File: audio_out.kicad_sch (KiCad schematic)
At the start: 34 parts, among them SW2 Gain0, SW3 Gain1, U3 PAM8908JER, U4 PCM5102A, U8 AP7333-33SRG-7

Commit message: Reviewing every item in the BOM against LCSC database. Found several errors already. Part way done.
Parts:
- C21, C22, C25, C27, C30, C31, C36, C37, C38, C39, C41, C42, C43: DPFNOTES (none) -> 25V 1uF X5R ±10% 0402 Multilayer Ceramic Capacitors MLCC - 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; JLC Basic Part (none) -> Basic
- C23, C24, C40: DPFNOTES (none) -> 50V 2.2uF X5R ±10% 0805 Multilayer Ceramic Capacitors MLCC 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; JLC Basic Part (none) -> Basic; Manu Part (none) -> CL21A225KBQNNNE
- C26, C28, C32, C33: DPFNOTES (none) -> 50V 100nF X7R ±10% 0402 Multilayer Ceramic Capacitors MLCC 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; JLC Basic Part (none) -> Basic
- C29, C34, C35: JLC Basic Part (none) -> Basic
- R21: JLC Basic Part (none) -> Basic; Manu Part (none) -> 0402WGF1002TCE; Manufacturer (none) -> UNI-ROYAL(Uniroyal Elec)

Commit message: Finished checking all parts against LCSC IDs. Found remaining errors. Added manufacturer part numbers to all parts.
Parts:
- C21, C22, C25, C27, C30, C31, C36, C37, C38, C39, C41, C42, C43: Manu Part (none) -> CL05A105KA5NQNC; Manufacturer (none) -> Samsung Electro-Mechanics
- C23, C24, C40: Manufacturer (none) -> Samsung Electro-Mechanics
- C26, C28, C32, C33: Manu Part (none) -> CL05B104KB54PNC; Manufacturer (none) -> Samsung Electro-Mechanics
- C29: Manu Part (none) -> CL10A106MA8NRNC; Manufacturer (none) -> Samsung Electro-Mechanics
- C34, C35: Manu Part (none) -> CL05B103KB5NNNC; Manufacturer (none) -> Samsung Electro-Mechanics
- R22, R23: JLC Basic Part (none) -> Basic; Manu Part (none) -> 0402WGF2200TCE; Manufacturer (none) -> UNI-ROYAL(Uniroyal Elec)
- R24, R25: JLC Basic Part (none) -> Extended; Manu Part (none) -> 0402WGF3901TCE; Manufacturer (none) -> UNI-ROYAL(Uniroyal Elec)
- RN1: JLC Basic Part (none) -> Extended; Manu Part (none) -> 4D03WGJ0560T5E; Manufacturer (none) -> UNI-ROYAL(Uniroyal Elec)
- SW2, SW3: DPFNOTES ALPSALPINE SSSS811101, Like C&K PCM-12-SMT PCM12SMTR -> ALPSALPINE SSSS811101, Like C&K PCM-12-SMT PCM12SMTR --- 30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; JLC Basic Part (none) -> Extended; Manu Part (none) -> SSSS811101; Manufacturer (none) -> ALPSALPINE
- U3: JLC Basic Part (none) -> Extended; Manu Part (none) -> PAM8908JER; Manufacturer (none) -> Diodes Incorporated
- U4: JLC Basic Part (none) -> Extended; Manu Part (none) -> PCM5102APWR; Manufacturer (none) -> Texas Instruments
- U8: DPFNOTES (none) -> 300mA 65dB@(100Hz) Fixed 3.3V Positive electrode 6V SOT-23 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; JLC Basic Part (none) -> Extended; Manu Part (none) -> AP7333-33SRG-7; Manufacturer (none) -> Diodes Incorporated

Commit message: Update schematic with notes on the headphone amplifier and I2S MCK
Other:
- note added: "Datasheet"
- note added: "Pimoroni"
- note added: "Pimoroni used a different INx- configuration; this is from the datasheet."
- note added: "Pullup to unmute audio when AUDIO_MUTE not driven"
- note added: "This chip does not need MCK. Leave it disconnected for simplicity."
- note added: "Why does Pimoroni use R1-4 on line inputs from PCM5102A DAC?"
- moved on the sheet: R21

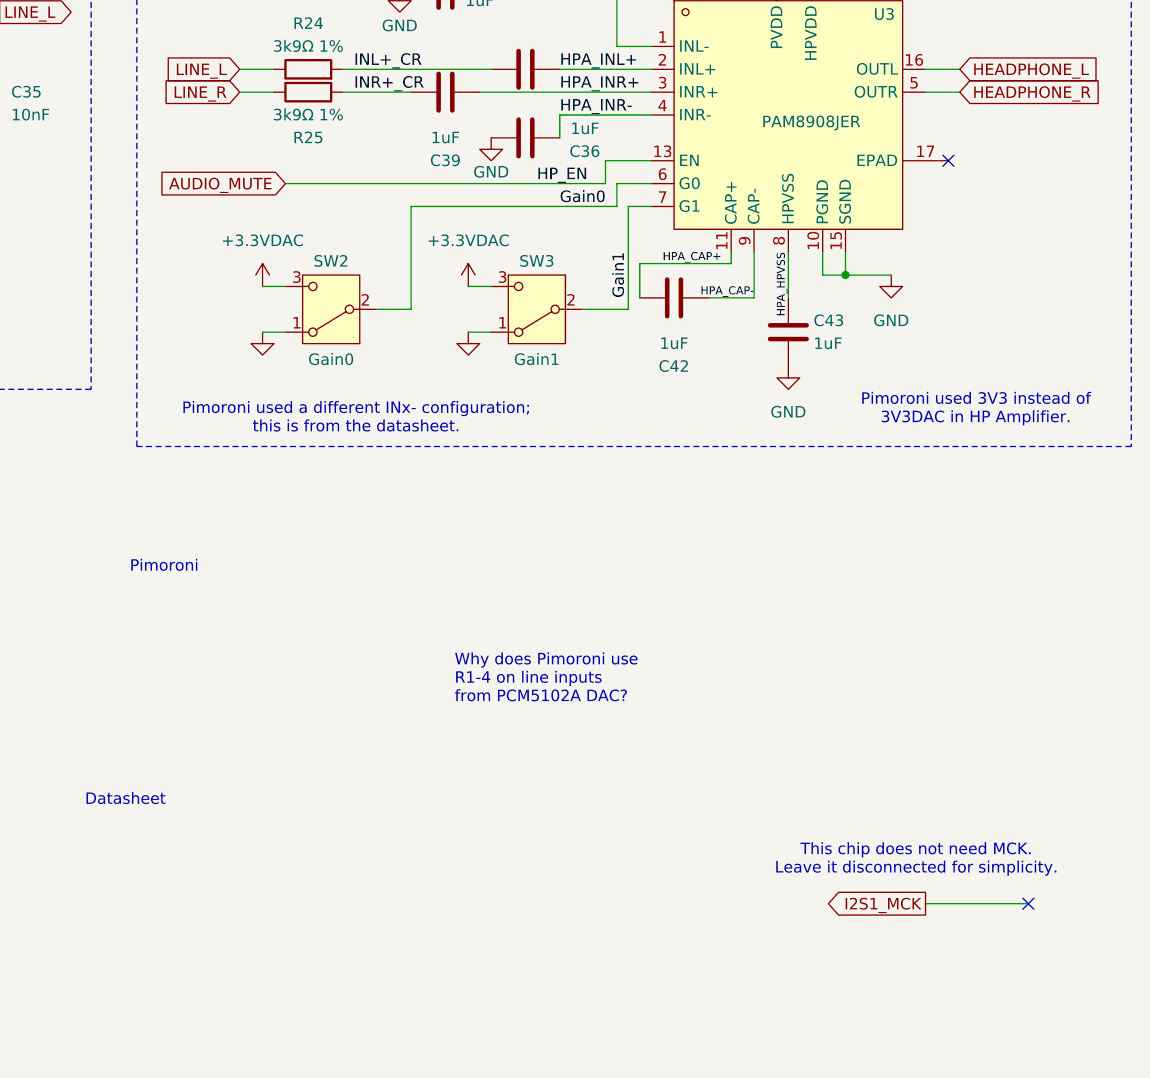
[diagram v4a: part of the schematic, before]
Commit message: More revisions for EVT2: 1. Move GAIN0/1 to MCU pins. 2. Revise SPI header with additional screen GPIO. 3. Revise GPIO header due to 1 and 2.
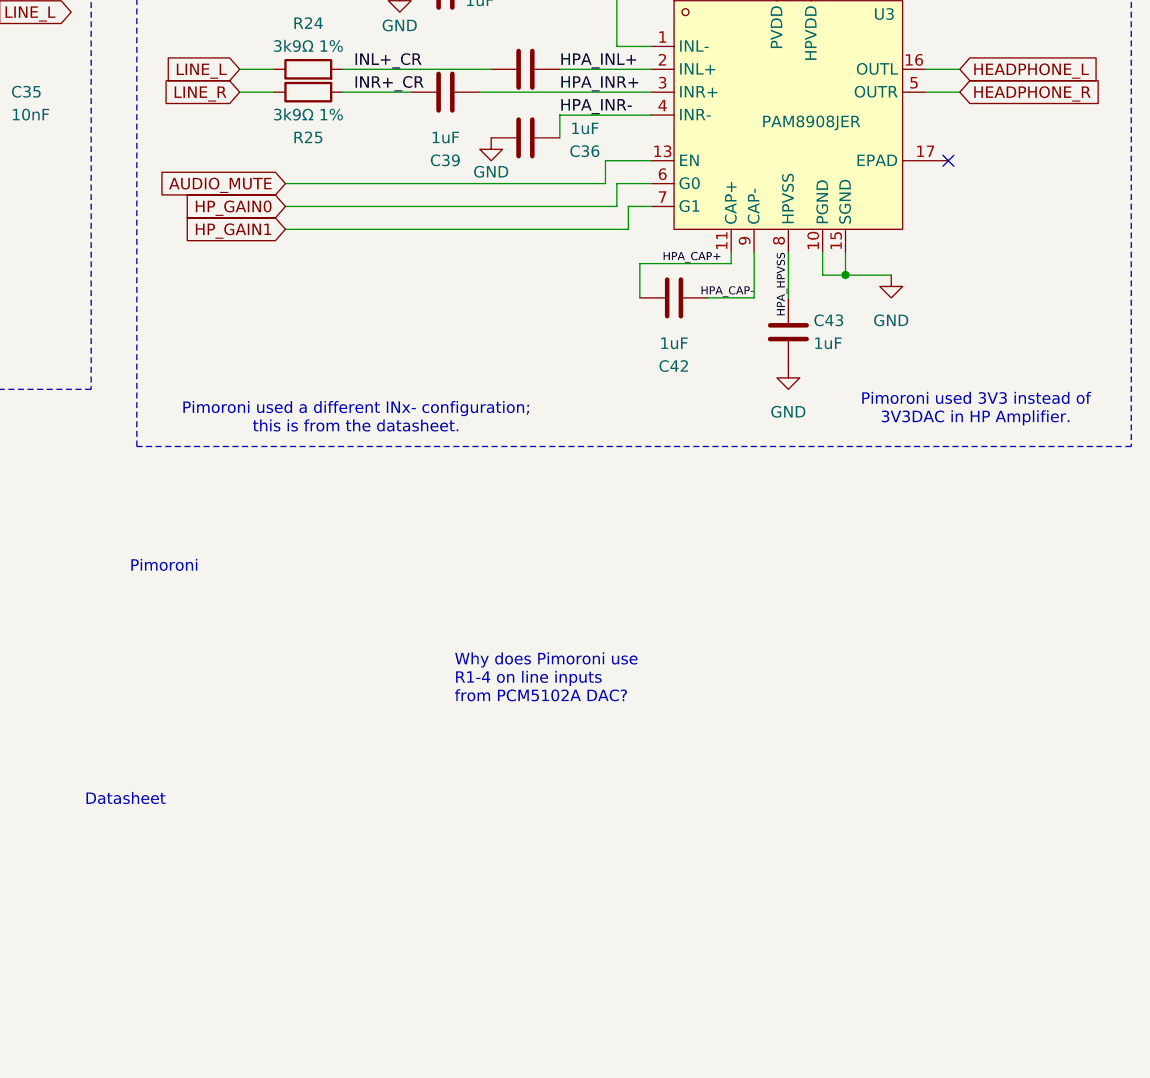
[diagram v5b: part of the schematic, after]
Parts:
- removed SW2: Gain0, Button_Switch_SMD:SW_SPDT_PCM12, symbol Switch:SW_SPDT
- removed SW3: Gain1, Button_Switch_SMD:SW_SPDT_PCM12, symbol Switch:SW_SPDT
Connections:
- net Gain0 renamed HP_GAIN0
- net Gain1 renamed HP_GAIN1
- no-connect marks 4 -> 3
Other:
- note removed: "This chip does not need MCK. Leave it disconnected for simplicity."
